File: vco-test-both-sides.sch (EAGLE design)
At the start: 25 parts, among them IC2 CEM3340

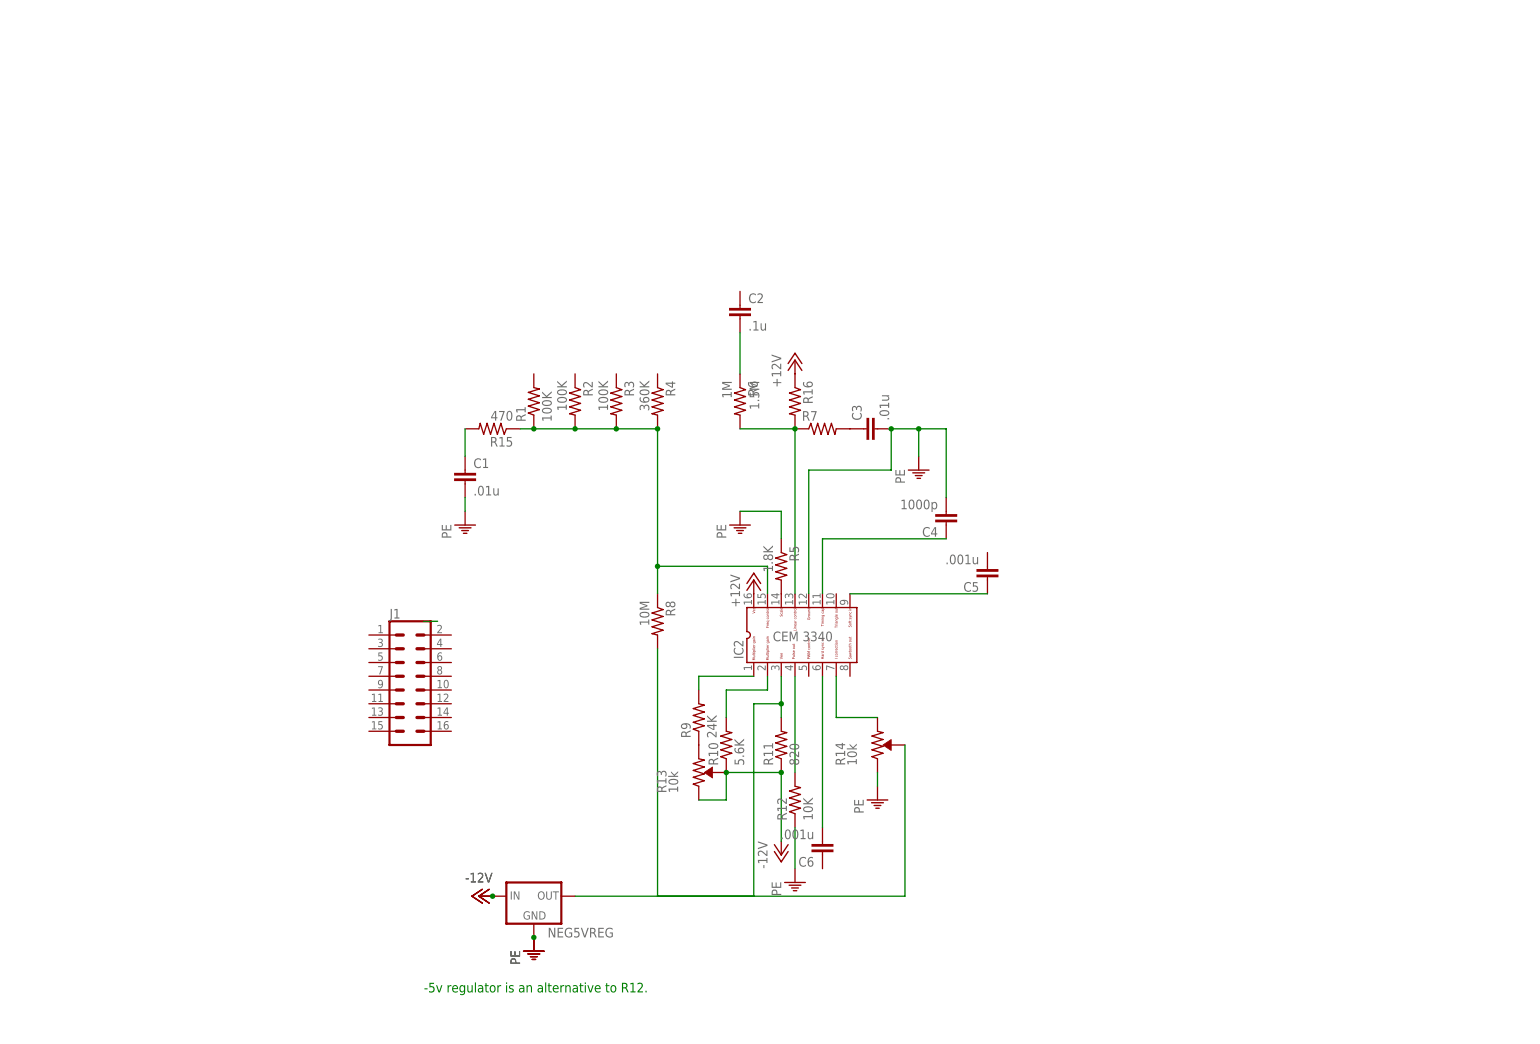
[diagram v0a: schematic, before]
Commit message: Added a new project (version), using both sides of board.
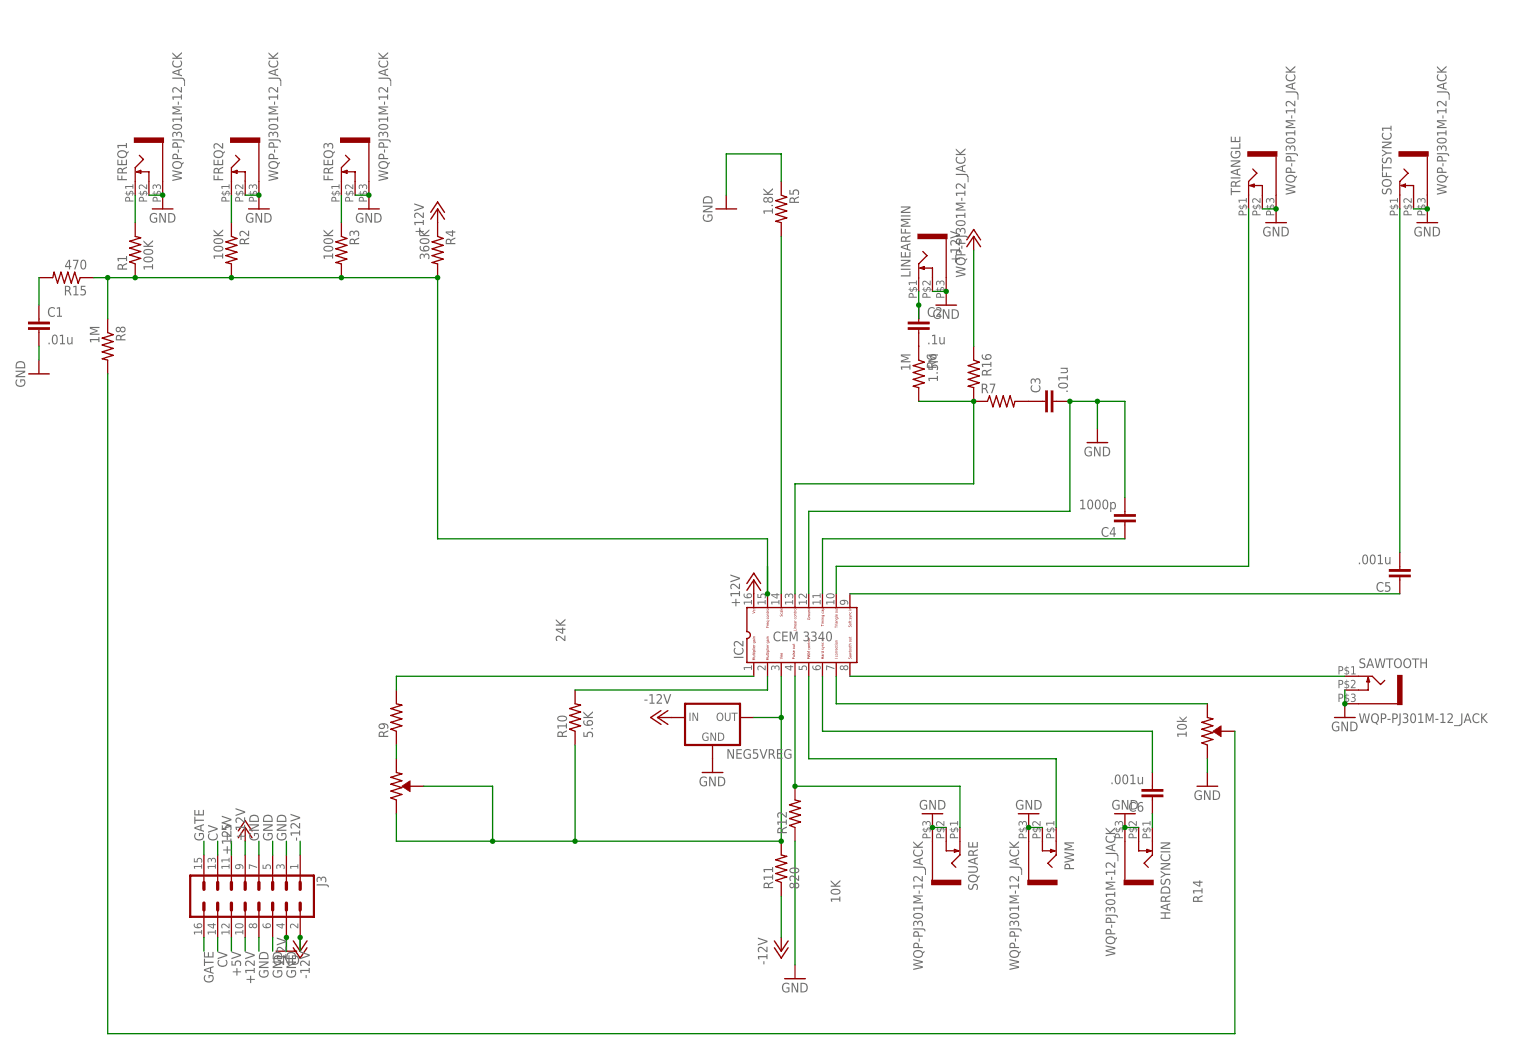
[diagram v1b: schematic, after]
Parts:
- removed J1: (no value), SparkFun-Connectors:CONN_08X2_SHROUD
- added FREQ1, FREQ2, FREQ3, HARDSYNCIN, LINEARFMIN, PWM, SAWTOOTH, SOFTSYNC1, SQUARE, TRIANGLE: WQP-PJ301M-12_JACK, thonkiconn:WQP-PJ301M-12_JACK
- added J3: (no value), SparkFun-Connectors:CONN_08X2_SHROUD
- R8: value 10M -> 1M
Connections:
- new net +5V: J3.11, J3.12
- new net CV: J3.13, J3.14
- new net GATE: J3.15, J3.16
- new net GND: C3.2, C4.2, FREQ1.1, FREQ1.3, FREQ2.1, FREQ2.3, FREQ3.1, FREQ3.3, HARDSYNCIN.1, HARDSYNCIN.3, IC2.12, J3.3, J3.4, J3.5, J3.6, J3.7, J3.8, LINEARFMIN.1, LINEARFMIN.3, NEG5VREG.GND, PWM.1, PWM.3, R12.1, R14.CW, SAWTOOTH.1, SAWTOOTH.3, SOFTSYNC1.1, SOFTSYNC1.3, SQUARE.1, SQUARE.3, TRIANGLE.1, TRIANGLE.3
- new net N$14: FREQ1.2, R1.2
- new net N$16: C6.1, HARDSYNCIN.2
- new net N$20: FREQ2.2, R2.1
- new net N$22: FREQ3.2, R3.1
- new net N$23: IC2.10, TRIANGLE.2
- new net N$24: C2.1, LINEARFMIN.2
- new net N$29: C5.2, SOFTSYNC1.2
- new net N$31: IC2.8, SAWTOOTH.2
- new net N$35: IC2.5, PWM.2
- net +12V: now also J3.10, J3.9, R4.1
- net -12V: now also J3.1, J3.2; no longer R10.1, R13.CW, R13.WIPER
- net N$12: now also R10.1, R13.CW, R13.WIPER
- net N$18: now also SQUARE.2
- net PE: no longer C3.2, C4.2, IC2.12, NEG5VREG.GND, R12.1, R14.CW
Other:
- note removed: "-5v regulator is an alternative to R12."
- moved on the sheet: C1, C2, C3, C4, C5, C6, NEG5VREG, R1, R10, R11, R12, R14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
